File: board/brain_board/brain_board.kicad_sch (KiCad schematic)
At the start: 9 parts, among them J1 Screw_Terminal_01x03, J2 Conn_02x04_Odd_Even, J3 Micro_SD_Card, M1 MountingHoles, U1 WeMos_D1_mini

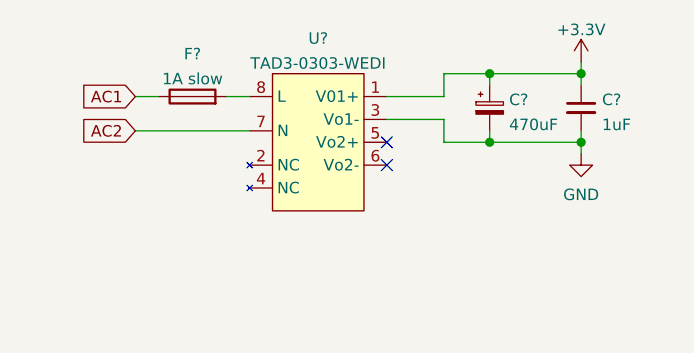
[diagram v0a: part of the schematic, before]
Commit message: Fix SD-Slot pin alignment
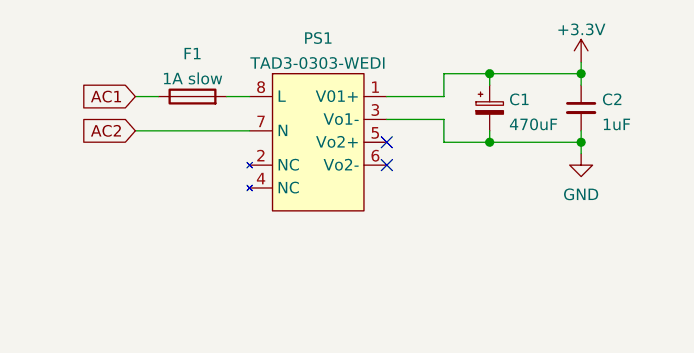
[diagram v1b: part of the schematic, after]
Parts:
- gave numbers to parts that had none: 4
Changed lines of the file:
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@@
   (symbol (lib_id "Device:Fuse") (at 109.22 22.86 90) (unit 1)
     (in_bom yes) (on_board yes) (fields_autoplaced)
-    (property "Reference" "F?" (id 0) (at 109.22 18.1314 90))
+    (property "Reference" "F1" (id 0) (at 109.22 18.1314 90))
     (property "Value" "1A slow" (id 1) (at 109.22 20.9065 90))
     (property "Footprint" "phase_angle_control:Fuse_2410" (id 2) (at 109.22 24.638 90)
@@
   (symbol (lib_id "Device:C_Polarized_Small") (at 142.24 24.13 0) (unit 1)
     (in_bom yes) (on_board yes) (fields_autoplaced)
-    (property "Reference" "C?" (id 0) (at 144.3991 23.2215 0)
+    (property "Reference" "C1" (id 0) (at 144.3991 23.2215 0)
       (effects (font (size 1.27 1.27)) (justify left))
     )
@@
   (symbol (lib_id "Device:C_Small") (at 152.4 24.13 0) (unit 1)
     (in_bom yes) (on_board yes) (fields_autoplaced)
-    (property "Reference" "C?" (id 0) (at 154.7242 23.2215 0)
+    (property "Reference" "C2" (id 0) (at 154.7242 23.2215 0)
       (effects (font (size 1.27 1.27)) (justify left))
     )
@@
   (symbol (lib_id "phase_angle_control:TAD3-0303-WEDI") (at 123.19 26.67 0) (unit 1)
     (in_bom yes) (on_board yes) (fields_autoplaced)
-    (property "Reference" "U?" (id 0) (at 123.19 16.4042 0))
+    (property "Reference" "PS1" (id 0) (at 123.19 16.4042 0))
     (property "Value" "TAD3-0303-WEDI" (id 1) (at 123.19 19.1793 0))
     (property "Footprint" "phase_angle_control:TAD3-0303-WEDI" (id 2) (at 123.19 17.78 0)
@@
     )
     (pin "1")
-    (pin "3")
-    (pin "4")
-    (pin "2")
+    (pin "2")
+    (pin "3")
+    (pin "4")
     (pin "5")
     (pin "6")
@@
       (effects (font (size 1.27 1.27)) hide)
     )
-    (property "Datasheet" "http://katalog.we-online.de/em/datasheet/693072010801.pdf" (id 3) (at 135.89 95.25 0)
+    (property "Datasheet" "https://datasheet.lcsc.com/lcsc/1912111437_HOAUC-HYC39-TF08-180_C341095.pdf" (id 3) (at 135.89 95.25 0)
       (effects (font (size 1.27 1.27)) hide)
     )
@@
       (reference "#PWR0110") (unit 1) (value "GND") (footprint "")
     )
+    (path "/535e7a01-4cda-4662-b434-cfc58bd6b027"
+      (reference "C1") (unit 1) (value "470uF") (footprint "Capacitor_THT:CP_Radial_D8.0mm_P3.50mm")
+    )
     (path "/42f47601-c933-441a-aab5-fbec539d2791"
-      (reference "C?") (unit 1) (value "1uF") (footprint "Capacitor_THT:C_Disc_D4.3mm_W1.9mm_P5.00mm")
-    )
-    (path "/535e7a01-4cda-4662-b434-cfc58bd6b027"
-      (reference "C?") (unit 1) (value "470uF") (footprint "Capacitor_THT:CP_Radial_D8.0mm_P3.50mm")
+      (reference "C2") (unit 1) (value "1uF") (footprint "Capacitor_THT:C_Disc_D4.3mm_W1.9mm_P5.00mm")
     )
     (path "/ed517eaa-8062-414f-89a0-0f5b65b9356f"
-      (reference "F?") (unit 1) (value "1A slow") (footprint "phase_angle_control:Fuse_2410")
+      (reference "F1") (unit 1) (value "1A slow") (footprint "phase_angle_control:Fuse_2410")
     )
     (path "/f2275004-8fcf-40a2-987c-89baec04c0dd"
@@
       (reference "M1") (unit 1) (value "MountingHoles") (footprint "pac:MountingHolesPE")
     )
+    (path "/eee51e1a-e165-417b-a331-54154ae9fdce"
+      (reference "PS1") (unit 1) (value "TAD3-0303-WEDI") (footprint "phase_angle_control:TAD3-0303-WEDI")
+    )
     (path "/f4c0ff89-3527-43d8-96ec-42c6b192926c"
       (reference "U1") (unit 1) (value "WeMos_D1_mini") (footprint "Module:WEMOS_D1_mini_light")
     )
-    (path "/eee51e1a-e165-417b-a331-54154ae9fdce"
-      (reference "U?") (unit 1) (value "TAD3-0303-WEDI") (footprint "phase_angle_control:TAD3-0303-WEDI")
-    )
-  )
+  )
